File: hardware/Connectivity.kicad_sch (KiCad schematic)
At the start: 67 parts, among them U1 MCP2542FD-E/MF, U11 LM397, U2 LM397, U5 LM397, U6 MCP2542FD-E/MF, U7 MCP2542FD-E/MF, U8 LM397, U9 LM397

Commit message: sync
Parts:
- removed C5, C72, C74, C76: 10nF, Capacitor_SMD:C_0603_1608Metric, symbol Device:C_Small
- removed C50, C66, C71, C73, C75, C77: 100nF, Capacitor_SMD:C_0603_1608Metric, symbol Device:C_Small
- removed R15, R17, R26, R32, R38, R39, R40, R41, R70, R71, R72, R73, R77, R78, R79, R80, R84, R85, R86, R87: 10k, Resistor_SMD:R_0603_1608Metric, symbol Device:R_Small
- removed R33, R35, R42, R43, R68, R69, R74, R75, R76, R81, R82, R83, R88, R89, R90: TBD, Resistor_SMD:R_0603_1608Metric, symbol Device:R_Small
- removed U11, U2, U5, U8, U9: LM397, Package_TO_SOT_SMD:SOT-23-5, symbol Comparator:LM397
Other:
- added sheet AIR Minus (InputSeperation.kicad_sch)
- added sheet AIR Plus (InputSeperation.kicad_sch)
- added sheet AIR Precharge (InputSeperation.kicad_sch)
- added sheet Input1 (InputSeperation.kicad_sch)
- added sheet Input2 (InputSeperation.kicad_sch)
- note added: "INPUT SEPERATION"
- note removed: "AIR DETECT"
- note removed: "MEDIUM VOLTAGE INPUTS"

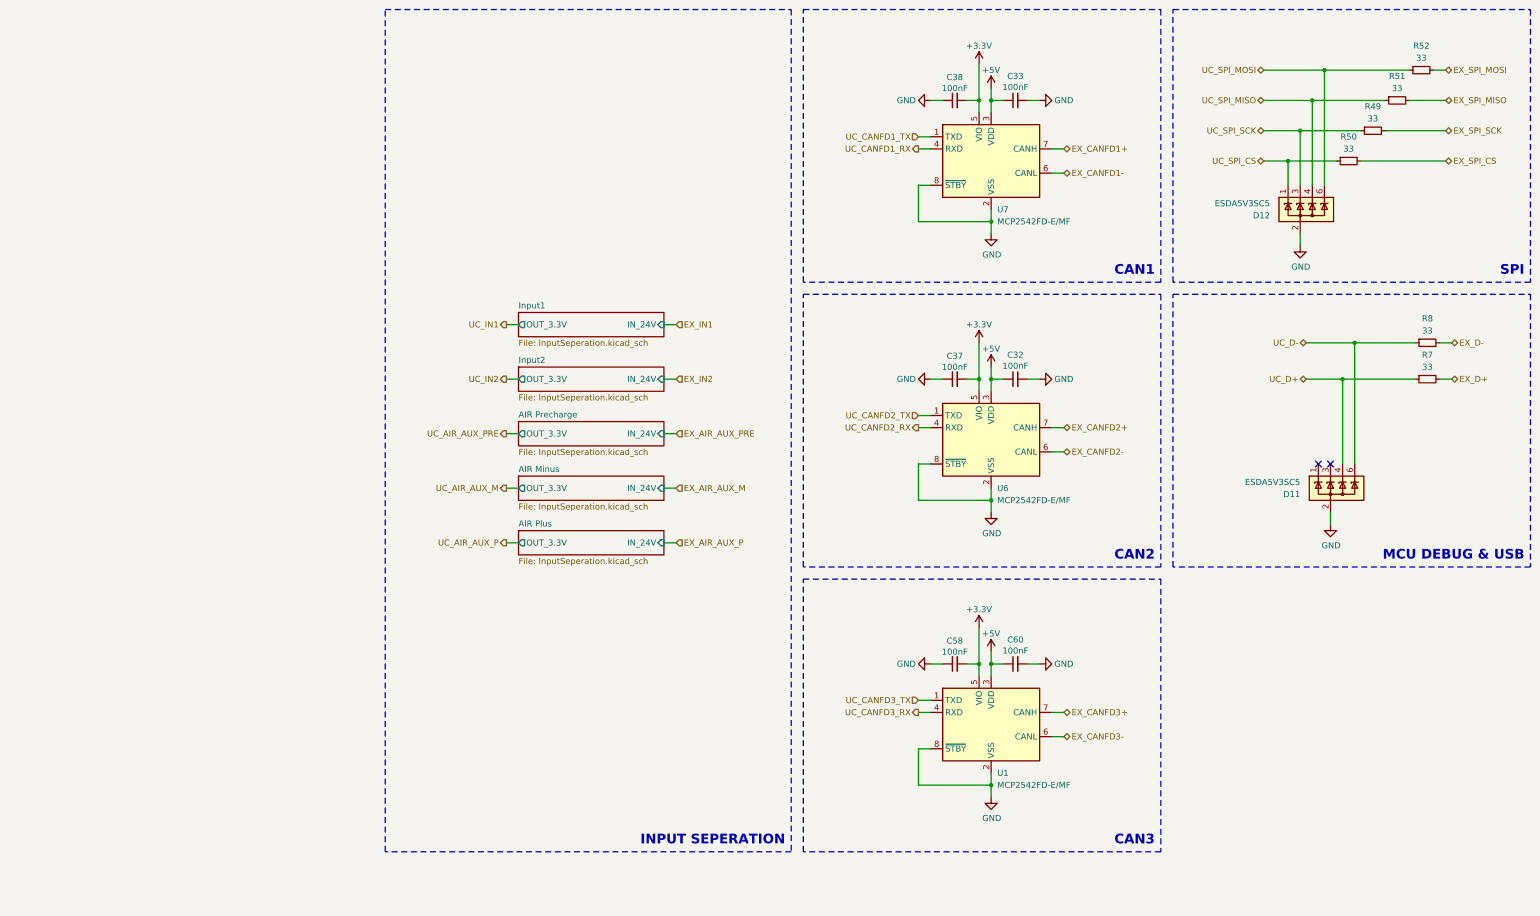
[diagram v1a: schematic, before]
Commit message: the connectors wil stay and wont be changed further
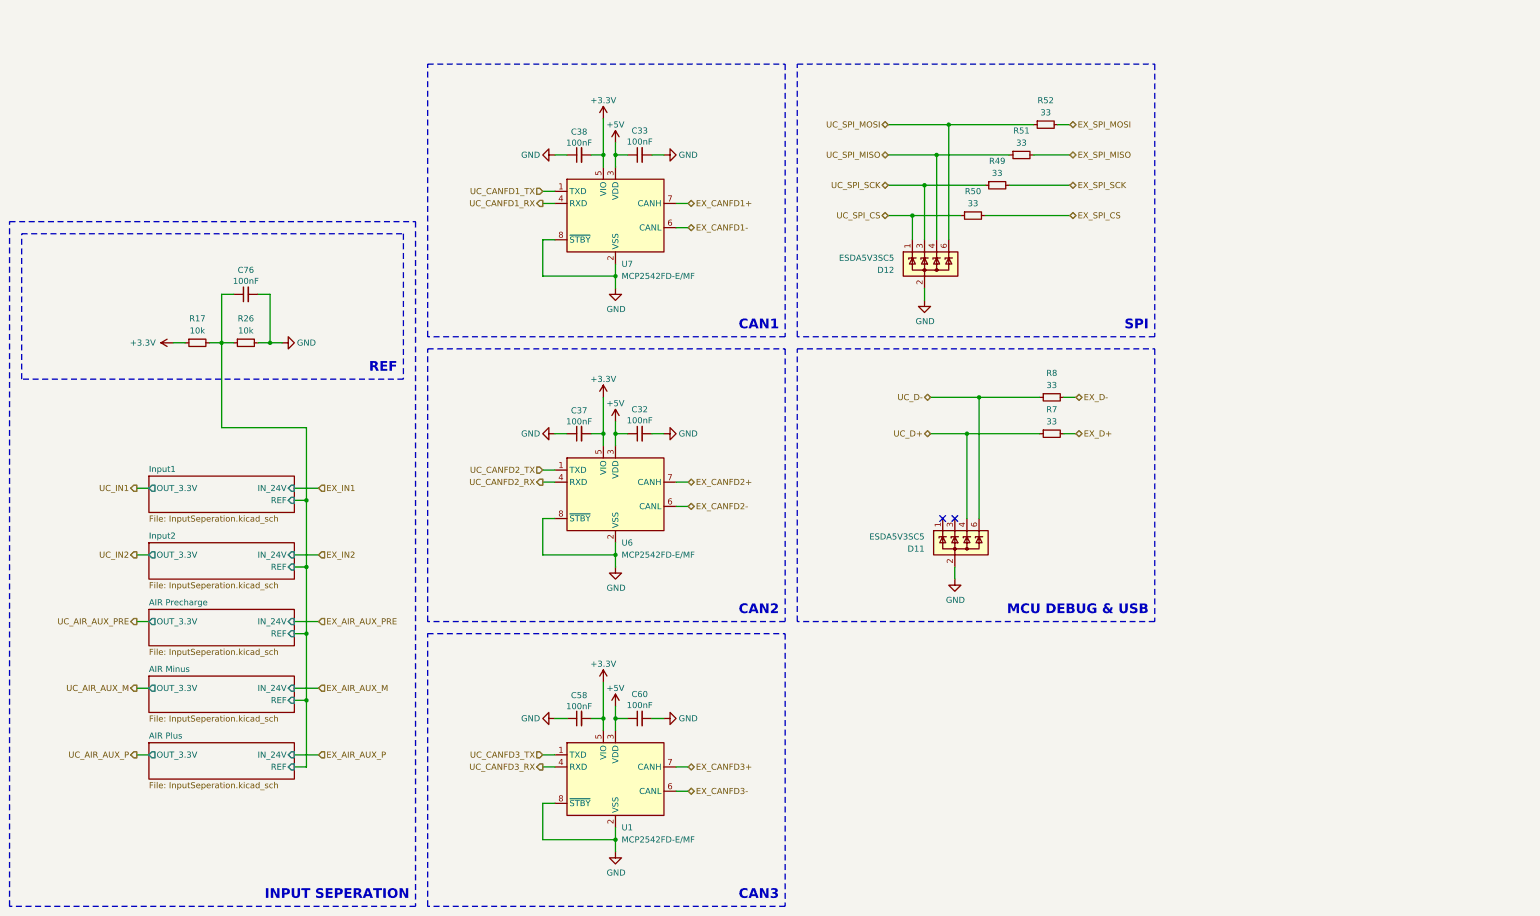
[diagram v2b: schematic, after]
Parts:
- added C76: 100nF, Capacitor_SMD:C_0603_1608Metric, symbol Device:C_Small
- added R17, R26: 10k, Resistor_SMD:R_0603_1608Metric, symbol Device:R_Small
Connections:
- net +3.3V: now also R17.1
- net GND: now also C76.2, R26.2
- new net AIR Minus/REF: C76.1, R17.2, R26.1
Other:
- sheet AIR Minus ports: added REF; removed none
- sheet AIR Plus ports: added REF; removed none
- sheet AIR Precharge ports: added REF; removed none
- sheet Input1 ports: added REF; removed none
- sheet Input2 ports: added REF; removed none
- note added: "REF"
- moved on the sheet: C32, C33, C37, C38, C58, C60, D11, D12, R49, R50, R51, R52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

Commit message: sync
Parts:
- added TP12, TP13, TP14, TP15, TP16: TestPoint_Small, TestPoint:TestPoint_THTPad_D1.0mm_Drill0.5mm, symbol Connector:TestPoint_Small
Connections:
- net UC_AIR_AUX_M: now also TP15.1
- net UC_AIR_AUX_P: now also TP16.1
- net UC_AIR_AUX_PRE: now also TP14.1
- net UC_IN1: now also TP12.1
- net UC_IN2: now also TP13.1

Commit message: some routing done
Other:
- note added: "MCU USB"
- note removed: "MCU DEBUG & USB"
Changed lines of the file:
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@@
 		)
 	)
-	(text "MCU DEBUG & USB"
+	(text "MCU USB"
 		(exclude_from_sim no)
 		(at 325.12 177.8 0)

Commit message: routing done, drc checked
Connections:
- net EX_D+: now also R8.2; no longer R7.2
- net EX_D-: now also R7.2; no longer R8.2
- net UC_D+: now also D11.6 (A), R8.1; no longer D11.4 (A), R7.1
- net UC_D-: now also D11.4 (A), R7.1; no longer D11.6 (A), R8.1
- net UC_SPI_MISO: now also D12.6 (A), R52.1; no longer D12.4 (A), R51.1
- net UC_SPI_MOSI: now also D12.3 (A), R49.1; no longer D12.6 (A), R52.1
- net UC_SPI_SCK: now also D12.4 (A), R51.1; no longer D12.3 (A), R49.1
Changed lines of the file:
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@@
 	(hierarchical_label "UC_D+"
 		(shape bidirectional)
+		(at 279.4 132.08 180)
+		(fields_autoplaced yes)
+		(effects
+			(font
+				(size 1.27 1.27)
+			)
+			(justify right)
+		)
+	)
+	(hierarchical_label "EX_SPI_SCK"
+		(shape bidirectional)
+		(at 308.61 87.63 0)
+		(fields_autoplaced yes)
+		(effects
+			(font
+				(size 1.27 1.27)
+			)
+			(justify left)
+		)
+	)
+	(hierarchical_label "UC_SPI_CS"
+		(shape bidirectional)
+		(at 270.51 93.98 180)
+		(fields_autoplaced yes)
+		(effects
+			(font
+				(size 1.27 1.27)
+			)
+			(justify right)
+		)
+	)
+	(hierarchical_label "EX_CANFD1-"
+		(shape bidirectional)
+		(at 228.6 96.52 0)
+		(fields_autoplaced yes)
+		(effects
+			(font
+				(size 1.27 1.27)
+			)
+			(justify left)
+		)
+	)
+	(hierarchical_label "EX_D+"
+		(shape bidirectional)
+		(at 309.88 132.08 0)
+		(fields_autoplaced yes)
+		(effects
+			(font
+				(size 1.27 1.27)
+			)
+			(justify left)
+		)
+	)
+	(hierarchical_label "UC_AIR_AUX_PRE"
+		(shape output)
+		(at 105.41 179.07 180)
+		(fields_autoplaced yes)
+		(effects
+			(font
+				(size 1.27 1.27)
+			)
+			(justify right)
+		)
+	)
+	(hierarchical_label "EX_CANFD2+"
+		(shape bidirectional)
+		(at 228.6 149.86 0)
+		(fields_autoplaced yes)
+		(effects
+			(font
+				(size 1.27 1.27)
+			)
+			(justify left)
+		)
+	)
+	(hierarchical_label "UC_IN1"
+		(shape output)
+		(at 105.41 151.13 180)
+		(fields_autoplaced yes)
+		(effects
+			(font
+				(size 1.27 1.27)
+			)
+			(justify right)
+		)
+	)
+	(hierarchical_label "UC_AIR_AUX_P"
+		(shape output)
+		(at 105.41 207.01 180)
+		(fields_autoplaced yes)
+		(effects
+			(font
+				(size 1.27 1.27)
+			)
+			(justify right)
+		)
+	)
+	(hierarchical_label "EX_AIR_AUX_M"
+		(shape input)
+		(at 151.13 193.04 0)
+		(fields_autoplaced yes)
+		(effects
+			(font
+				(size 1.27 1.27)
+			)
+			(justify left)
+		)
+	)
+	(hierarchical_label "UC_D-"
+		(shape bidirectional)
 		(at 279.4 139.7 180)
 		(fields_autoplaced yes)
@@
 		)
 	)
-	(hierarchical_label "EX_SPI_SCK"
-		(shape bidirectional)
-		(at 308.61 87.63 0)
-		(fields_autoplaced yes)
-		(effects
-			(font
-				(size 1.27 1.27)
-			)
-			(justify left)
-		)
-	)
-	(hierarchical_label "UC_SPI_CS"
-		(shape bidirectional)
-		(at 270.51 93.98 180)
-		(fields_autoplaced yes)
-		(effects
-			(font
-				(size 1.27 1.27)
-			)
-			(justify right)
-		)
-	)
-	(hierarchical_label "EX_CANFD1-"
-		(shape bidirectional)
-		(at 228.6 96.52 0)
-		(fields_autoplaced yes)
-		(effects
-			(font
-				(size 1.27 1.27)
-			)
-			(justify left)
-		)
-	)
-	(hierarchical_label "EX_D+"
+	(hierarchical_label "UC_SPI_MOSI"
+		(shape bidirectional)
+		(at 270.51 87.63 180)
+		(fields_autoplaced yes)
+		(effects
+			(font
+				(size 1.27 1.27)
+			)
+			(justify right)
+		)
+	)
+	(hierarchical_label "EX_IN1"
+		(shape input)
+		(at 151.13 151.13 0)
+		(fields_autoplaced yes)
+		(effects
+			(font
+				(size 1.27 1.27)
+			)
+			(justify left)
+		)
+	)
+	(hierarchical_label "EX_D-"
 		(shape bidirectional)
 		(at 309.88 139.7 0)
@@
 		)
 	)
-	(hierarchical_label "UC_AIR_AUX_PRE"
-		(shape output)
-		(at 105.41 179.07 180)
-		(fields_autoplaced yes)
-		(effects
-			(font
-				(size 1.27 1.27)
-			)
-			(justify right)
-		)
-	)
-	(hierarchical_label "EX_CANFD2+"
-		(shape bidirectional)
-		(at 228.6 149.86 0)
-		(fields_autoplaced yes)
-		(effects
-			(font
-				(size 1.27 1.27)
-			)
-			(justify left)
-		)
-	)
-	(hierarchical_label "UC_IN1"
-		(shape output)
-		(at 105.41 151.13 180)
-		(fields_autoplaced yes)
-		(effects
-			(font
-				(size 1.27 1.27)
-			)
-			(justify right)
-		)
-	)
-	(hierarchical_label "UC_AIR_AUX_P"
-		(shape output)
-		(at 105.41 207.01 180)
-		(fields_autoplaced yes)
-		(effects
-			(font
-				(size 1.27 1.27)
-			)
-			(justify right)
-		)
-	)
-	(hierarchical_label "EX_AIR_AUX_M"
-		(shape input)
-		(at 151.13 193.04 0)
-		(fields_autoplaced yes)
-		(effects
-			(font
-				(size 1.27 1.27)
-			)
-			(justify left)
-		)
-	)
-	(hierarchical_label "UC_D-"
-		(shape bidirectional)
-		(at 279.4 132.08 180)
-		(fields_autoplaced yes)
-		(effects
-			(font
-				(size 1.27 1.27)
-			)
-			(justify right)
-		)
-	)
-	(hierarchical_label "UC_SPI_MOSI"
+	(hierarchical_label "UC_CANFD3_RX"
+		(shape output)
+		(at 198.12 209.55 180)
+		(fields_autoplaced yes)
+		(effects
+			(font
+				(size 1.27 1.27)
+			)
+			(justify right)
+		)
+	)
+	(hierarchical_label "UC_CANFD3_TX"
+		(shape input)
+		(at 198.12 207.01 180)
+		(fields_autoplaced yes)
+		(effects
+			(font
+				(size 1.27 1.27)
+			)
+			(justify right)
+		)
+	)
+	(hierarchical_label "UC_CANFD2_TX"
+		(shape input)
+		(at 198.12 147.32 180)
+		(fields_autoplaced yes)
+		(effects
+			(font
+				(size 1.27 1.27)
+			)
+			(justify right)
+		)
+	)
+	(hierarchical_label "EX_SPI_MISO"
+		(shape bidirectional)
+		(at 308.61 81.28 0)
+		(fields_autoplaced yes)
+		(effects
+			(font
+				(size 1.27 1.27)
+			)
+			(justify left)
+		)
+	)
+	(hierarchical_label "UC_SPI_SCK"
+		(shape bidirectional)
+		(at 270.51 81.28 180)
+		(fields_autoplaced yes)
+		(effects
+			(font
+				(size 1.27 1.27)
+			)
+			(justify right)
+		)
+	)
+	(hierarchical_label "UC_SPI_MISO"
 		(shape bidirectional)
 		(at 270.51 74.93 180)
 		(fields_autoplaced yes)
 		(effects
-			(font
-				(size 1.27 1.27)
-			)
-			(justify right)
-		)
-	)
-	(hierarchical_label "EX_IN1"
-		(shape input)
-		(at 151.13 151.13 0)
-		(fields_autoplaced yes)
-		(effects
-			(font
-				(size 1.27 1.27)
-			)
-			(justify left)
-		)
-	)
-	(hierarchical_label "EX_D-"
-		(shape bidirectional)
-		(at 309.88 132.08 0)
-		(fields_autoplaced yes)
-		(effects
-			(font
-				(size 1.27 1.27)
-			)
-			(justify left)
-		)
-	)
-	(hierarchical_label "UC_CANFD3_RX"
-		(shape output)
-		(at 198.12 209.55 180)
-		(fields_autoplaced yes)
-		(effects
-			(font
-				(size 1.27 1.27)
-			)
-			(justify right)
-		)
-	)
-	(hierarchical_label "UC_CANFD3_TX"
-		(shape input)
-		(at 198.12 207.01 180)
-		(fields_autoplaced yes)
-		(effects
-			(font
-				(size 1.27 1.27)
-			)
-			(justify right)
-		)
-	)
-	(hierarchical_label "UC_CANFD2_TX"
-		(shape input)
-		(at 198.12 147.32 180)
-		(fields_autoplaced yes)
-		(effects
-			(font
-				(size 1.27 1.27)
-			)
-			(justify right)
-		)
-	)
-	(hierarchical_label "EX_SPI_MISO"
-		(shape bidirectional)
-		(at 308.61 81.28 0)
-		(fields_autoplaced yes)
-		(effects
-			(font
-				(size 1.27 1.27)
-			)
-			(justify left)
-		)
-	)
-	(hierarchical_label "UC_SPI_SCK"
-		(shape bidirectional)
-		(at 270.51 87.63 180)
-		(fields_autoplaced yes)
-		(effects
-			(font
-				(size 1.27 1.27)
-			)
-			(justify right)
-		)
-	)
-	(hierarchical_label "UC_SPI_MISO"
-		(shape bidirectional)
-		(at 270.51 81.28 180)
-		(fields_autoplaced yes)
-		(effects

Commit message: qfn mcu instead of bga sadge ;-;
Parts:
- removed C58, C60: 100nF, Capacitor_SMD:C_0603_1608Metric, symbol Device:C_Small
- removed U1: MCP2542FD-E/MF, Package_DFN_QFN:DFN-8-1EP_3x3mm_P0.65mm_EP1.55x2.4mm, symbol Interface_CAN_LIN:MCP2542FDxMF
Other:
- note removed: "CAN3"

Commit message: sync;
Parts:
- removed TP12, TP13, TP14, TP15, TP16: TestPoint_Small, TestPoint:TestPoint_THTPad_D1.0mm_Drill0.5mm, symbol Connector:TestPoint_Small
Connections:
- net EX_D+: now also R7.2; no longer R8.2
- net EX_D-: now also R8.2; no longer R7.2
- net UC_D+: now also D11.4 (A), R7.1; no longer D11.6 (A), R8.1
- net UC_D-: now also D11.6 (A), R8.1; no longer D11.4 (A), R7.1
